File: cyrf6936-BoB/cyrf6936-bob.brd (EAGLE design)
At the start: 18.4 x 30.7 mm, 23 parts

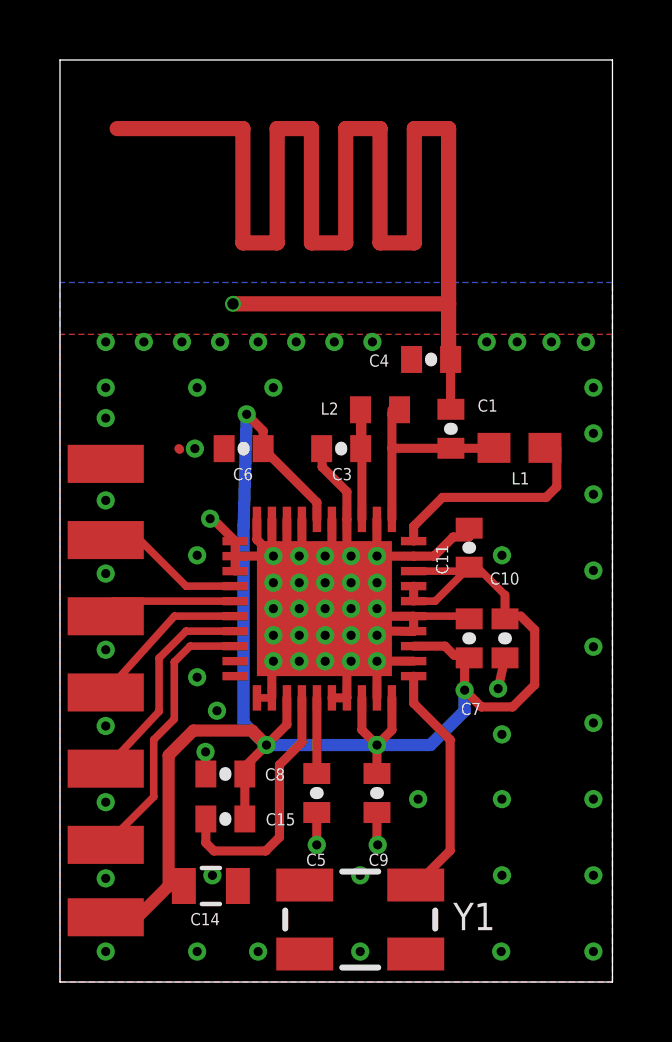
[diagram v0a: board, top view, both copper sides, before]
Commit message: restructured to try to keep track of various production files.  also,  tuned panel for vscore.
restructured to try to keep track of various production files.
tuned panel for vscore.
Cleaned up cyrf6936-bob to mask solder mask from the antenna area.
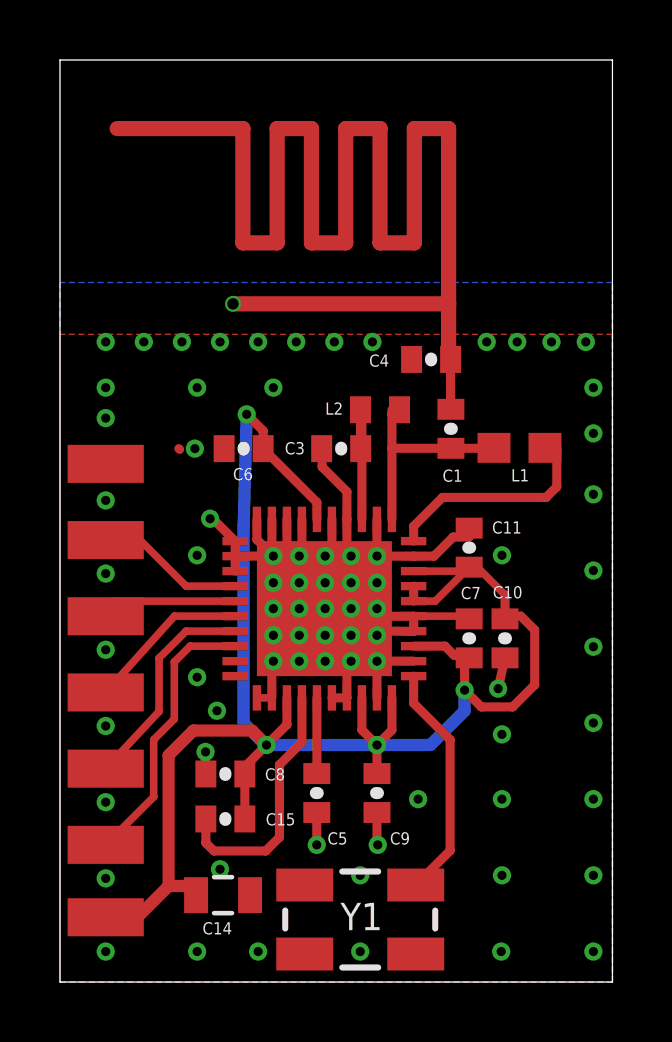
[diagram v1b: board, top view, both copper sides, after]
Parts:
- moved C14 0.51 mm to (14.3, 10.3)
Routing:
- net VCC: track 60.4 -> 60.9 mm

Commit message: Screwed up that last commit.  this update include changes to the production gerber folders.  Adds hackvana to the cyrf6936-BoB and cleans up the fab notes a bit.  Still need to standardize and parameterize the creation of the gerbers.
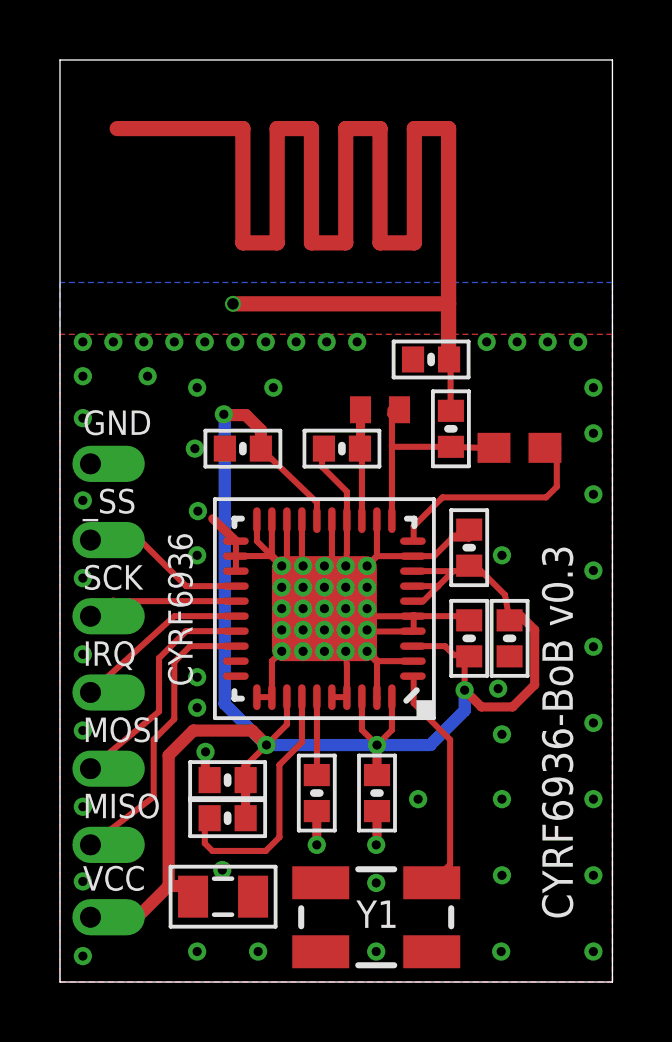
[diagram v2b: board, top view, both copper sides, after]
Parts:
- C1, C10, C11, C15, C3, C4, C5, C6, C7, C8, C9: device SparkFun-Passives:0402-CAP -> JCM-Capacitors:0402-CAP
- C14: device SparkFun-Passives:0805 -> JCM-Capacitors:0805
- CYRF6936: value CYRF6936 -> CYRF6936QFN; device JCM:QFN40 -> JCM-IC:QFN50P600X600X90-41N
- GND, IRQ, MISO, MOSI, SCK, VCC, _SS: value SOLDER_PAD -> SOLDER_PADTH; device JCM:SOLDER_PAD -> JCM-Connectors:1X1_50MIL
- moved Y1 0.54 mm to (19.4, 9.53)
- moved GND 0.51 mm to (9.91, 24.6)
- moved IRQ 0.51 mm to (9.91, 17.0)
- moved MISO 0.51 mm to (9.91, 11.9)
- moved MOSI 0.51 mm to (9.91, 14.5)
- moved SCK 0.51 mm to (9.91, 19.6)
- moved VCC 0.51 mm to (9.91, 9.53)
- moved _SS 0.51 mm to (9.91, 22.1)
- moved C8 0.22 mm to (14.5, 14.1)
- moved C10 0.15 mm to (23.9, 18.8)
- moved C15 0.08 mm to (14.5, 12.8)
- moved C14 0.05 mm to (14.3, 10.2)
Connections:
- net GND: now also CYRF6936.41, GND.P$1; no longer CYRF6936.GND, GND.SPAD
- net IRQ: now also IRQ.P$1; no longer IRQ.SPAD
- net MISO: now also MISO.P$1; no longer MISO.SPAD
- net MOSI: now also MOSI.P$1; no longer MOSI.SPAD
- net SCK: now also SCK.P$1; no longer SCK.SPAD
- net VCC: now also VCC.P$1; no longer VCC.SPAD
- net _SS: now also _SS.P$1; no longer _SS.SPAD
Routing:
- net VCC: track 60.9 -> 62.5 mm
- net GND: track 93.1 -> 91.7 mm, vias 78 -> 81
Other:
- board text added: "CYRF6936-BoB v0.3"
- board text added: "J Moreland Engineering LLC 15 Apr 2013"
- board text removed: "CYRF6936-BoB v0.1"
- board text removed: "J Moreland Engineering LLC 18 Apr 2013"
